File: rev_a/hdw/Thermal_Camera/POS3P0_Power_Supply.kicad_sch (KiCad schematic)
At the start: 0 parts

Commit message: changed a lot of circuits from +3.3V to +3.0V VDD
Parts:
- added C?: 10nF, Capacitors_SMD:C_0603, symbol Custom_Library:C_Custom
- added C? (x4): 10uF, Capacitors_SMD:C_1206, symbol Custom_Library:C_Custom
- added C? (x2): 0.1uF, Capacitors_SMD:C_0603, symbol Custom_Library:C_Custom
- added C?: 10uF, Capacitors_SMD:C_0603, symbol Custom_Library:C_Custom
- added D?: BAT48JFILM, Diode_SMD:D_SOD-323, symbol Diode:BAT48JFILM
- added L?: 2.2uH, Inductors_SMD:L_Vishay_IHLP-2020, symbol Custom_Library:L_Custom
- added Q?: BSS214NW, Package_TO_SOT_SMD:SOT-323_SC-70, symbol Transistor_FET:BSS214NW
- added Q?: ZXMS6004FFTA, Package_TO_SOT_SMD:SOT-23, symbol Custom_Library:ZXMS6004FFTA
- added R? (x3): 10k, Resistors_SMD:R_0603, symbol Custom_Library:R_Custom
- added R?: 3.16k, Resistors_SMD:R_0603, symbol Custom_Library:R_Custom
- added R?: 1.15k, Resistors_SMD:R_0603, symbol Custom_Library:R_Custom
- added R?: 10, Resistors_SMD:R_0603, symbol Custom_Library:R_Custom
- added TP?: TP, Custom Footprints Library:Test_Point, symbol Custom_Library:TP
- added U?: TPS62130A, Package_DFN_QFN:QFN-16-1EP_3x3mm_P0.5mm_EP1.75x1.75mm, symbol Custom_Library:TPS62130
- added U?: 74LVC1G97, Package_TO_SOT_SMD:SOT-363_SC-70-6, symbol Custom_Library:74LVC1G97_Power_AND
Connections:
- new net: C?.1, D?.1 (K), R?.1
- new net: Q?.1 (G), Q?.3 (D), R?.2
- new net: C?.1, U?.9 (SS/TR)
- new net: R?.1, R?.2, U?.5 (FB)
- new net: L?.1, U?.1 (SW), U?.2 (SW), U?.3 (SW)
- new net: R?.2, U?.4 (PG), U?.6
- new net +3.0V: C?.1, C?.1, C?.1, D?.2 (A), L?.2, Q?.3 (D), R?.1, R?.1, TP?.1 (TP), U?.14 (VOS), U?.5 (VCC)
- new net GND: C?.2, C?.2, C?.2, C?.2, C?.2, C?.2, C?.2, C?.2, Q?.2 (S), Q?.2 (S), R?.2, R?.2, U?.1 (GND), U?.15 (PGND), U?.16 (PGND), U?.17 (EP), U?.2 (GND), U?.6 (AGND), U?.7 (FSW), U?.8 (DEF)
- new net POS12_PGOOD: R?.1
- new net POS3P0_PGOOD: R?.1, U?.4
- new net POS3P0_RUN: Q?.1 (G), R?.2, U?.13 (EN), U?.3
- new net VBAT: C?.1, C?.1, C?.1, U?.10 (AVIN), U?.11 (PVIN), U?.12 (PVIN)
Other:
- note added: "figure out sequencing"

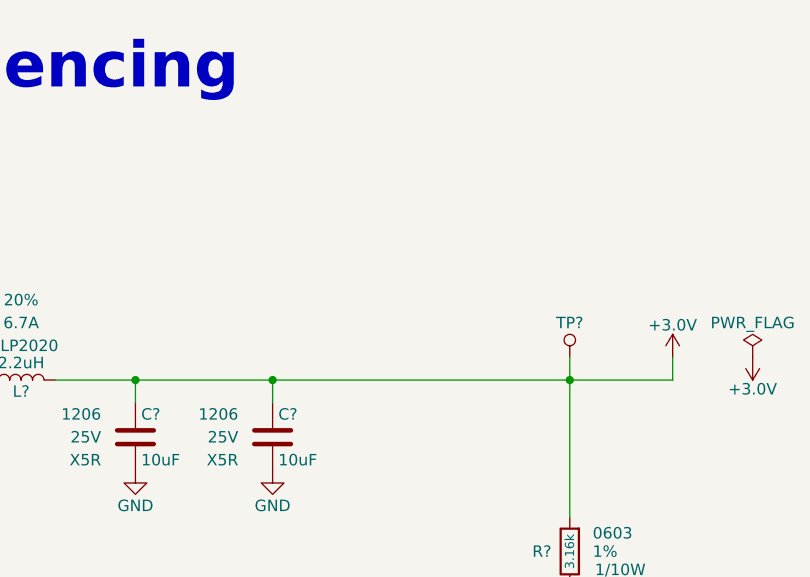
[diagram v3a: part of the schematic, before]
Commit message: added new telemetry circuits
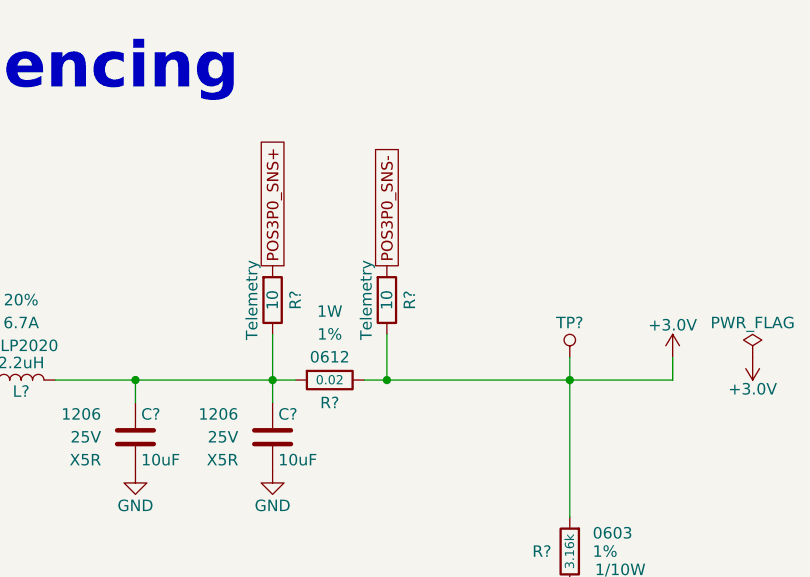
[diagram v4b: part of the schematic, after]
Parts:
- added R?: 0.02, Resistors_SMD:R_0612, symbol Custom_Library:R_Custom
- added R? (x2): 10, Resistors_SMD:R_0603, symbol Custom_Library:R_Custom
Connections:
- net +3.0V: now also R?.2, R?.2; no longer C?.1, C?.1, L?.2
- new net: C?.1, C?.1, L?.2, R?.1, R?.2
- new net POS3P0_SNS+: R?.1
- new net POS3P0_SNS-: R?.1

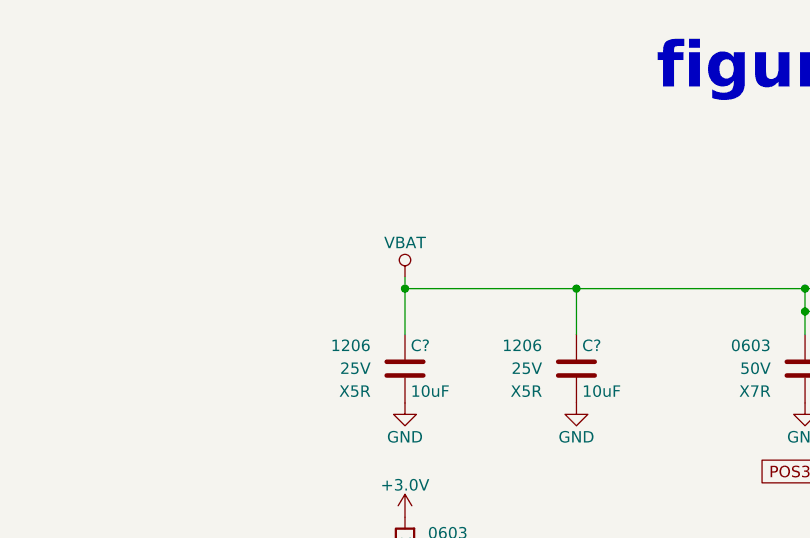
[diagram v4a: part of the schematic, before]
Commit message: added battery circuitry, LCD backlight
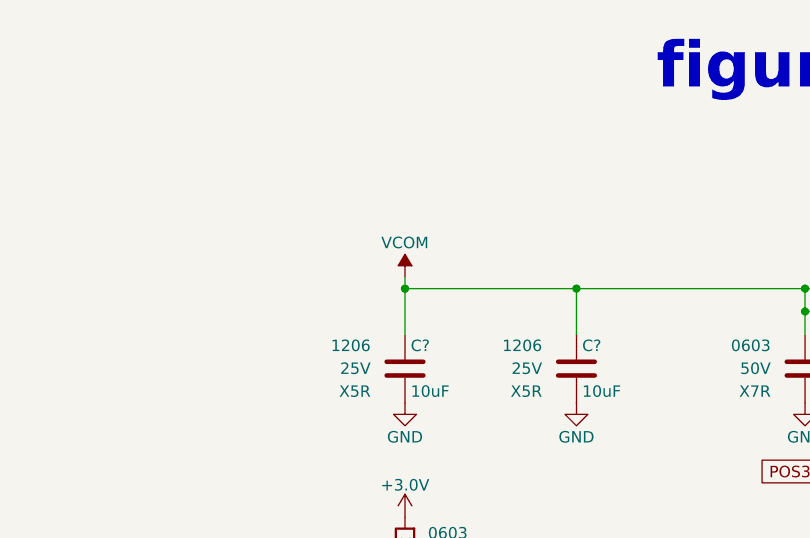
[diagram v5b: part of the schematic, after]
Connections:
- net VBAT renamed VCOM
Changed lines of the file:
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@@
-    )
-  )
-  (symbol (lib_id "Custom Library:VBAT") (at 73.66 48.26 0) (unit 1)
-    (in_bom yes) (on_board yes) (dnp no)
-    (property "Reference" "#PWR0625" (at 73.66 52.07 0)
-      (effects (font (size 1.27 1.27)) hide)
-    )
-    (property "Value" "VBAT" (at 73.66 44.45 0)
-      (effects (font (size 1.27 1.27)))
-    )
-    (property "Footprint" "" (at 73.66 48.26 0)
-      (effects (font (size 1.27 1.27)) hide)
-    )
-    (property "Datasheet" "" (at 73.66 48.26 0)
-      (effects (font (size 1.27 1.27)) hide)
-    )
-    (pin "1")
-    (instances
-      (project "Thermal_Camera"
-        (path "/4bd21e0b-5408-4b93-866e-c82ac5b31fa9/3fa2ed45-8dc3-4842-ae64-2bab78bff715"
-          (reference "#PWR0625") (unit 1)
-        )
-        (path "/4bd21e0b-5408-4b93-866e-c82ac5b31fa9/3996b81d-92d5-40b5-9537-6a34278c1c5b"
-          (reference "#PWR0406") (unit 1)
-        )
-      )
     )
   )
@@
         )
       )
+    )
+  )
+  (symbol (lib_id "power:VCOM") (at 73.66 48.26 0) (unit 1)
+    (in_bom yes) (on_board yes) (dnp no)
+    (property "Reference" "#PWR015" (at 73.66 52.07 0)
+      (effects (font (size 1.27 1.27)) hide)
+    )
+    (property "Value" "VCOM" (at 73.66 44.45 0)
+      (effects (font (size 1.27 1.27)))
+    )
+    (property "Footprint" "" (at 73.66 48.26 0)
+      (effects (font (size 1.27 1.27)) hide)
+    )
+    (property "Datasheet" "" (at 73.66 48.26 0)
+      (effects (font (size 1.27 1.27)) hide)
+    )
+    (pin "1")
+    (instances
+      (project "Thermal_Camera"
+        (path "/4bd21e0b-5408-4b93-866e-c82ac5b31fa9/079d68a7-d67d-4f5f-9c02-dfffe75c3c82"
+          (reference "#PWR015") (unit 1)
+        )
+        (path "/4bd21e0b-5408-4b93-866e-c82ac5b31fa9/3996b81d-92d5-40b5-9537-6a34278c1c5b"
+          (reference "#PWR012") (unit 1)
+        )
+      )

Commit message: lots of random schematic progress
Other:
- note removed: "figure out sequencing"
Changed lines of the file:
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@@
     (stroke (width 0) (type default))
-  )
-  (text "figure out sequencing" (at 101.6 27.94 0)
-    (effects (font (size 5.08 5.08) (thickness 1.016) bold (color 194 0 0 1)) (justify left bottom))
   )
   (global_label "POS3P0_RUN" (shape output) (at 49.53 168.91 0) (fields_autoplaced)
